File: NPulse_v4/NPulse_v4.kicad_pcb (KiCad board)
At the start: 4 copper layers, 39.8 x 72.5 mm, 163 parts, among them IC1 TXU0202QDCUR, IC2 DRV8220DSGR, IC3 DRV8220DSGR, IC4 DRV8220DSGR, IC5 DRV8220DSGR, IC6 DRV8220DSGR, IC7 DRV8220DSGR, IC8 DRV8220DSGR, IC9 DRV8220DSGR, J10 Conn_02x05_Odd_Even, J2 Conn_01x04_Pin, J3 Conn_01x06_Pin, J4 Conn_01x04_Pin, J5 Conn_02x05_Odd_Even, J6 Conn_02x05_Odd_Even, J7 Conn_02x05_Odd_Even, J8 Conn_02x05_Odd_Even, J9 Conn_02x05_Odd_Even, Q1 PMOS, Q2 NMOS, SW1 SW_Push, SW2 SW_SPDT, U1 STM32G484METx, U10 TPS7A0533PDBZ, U2 SN74LVC002, U3 SN74LVC002, U4 SN74LVC002, U5 SN74LVC002, U6 SN74LVC002, U7 SN74LVC002, U8 SN74LVC002, U9 SN74LVC002, Y1 16MHz

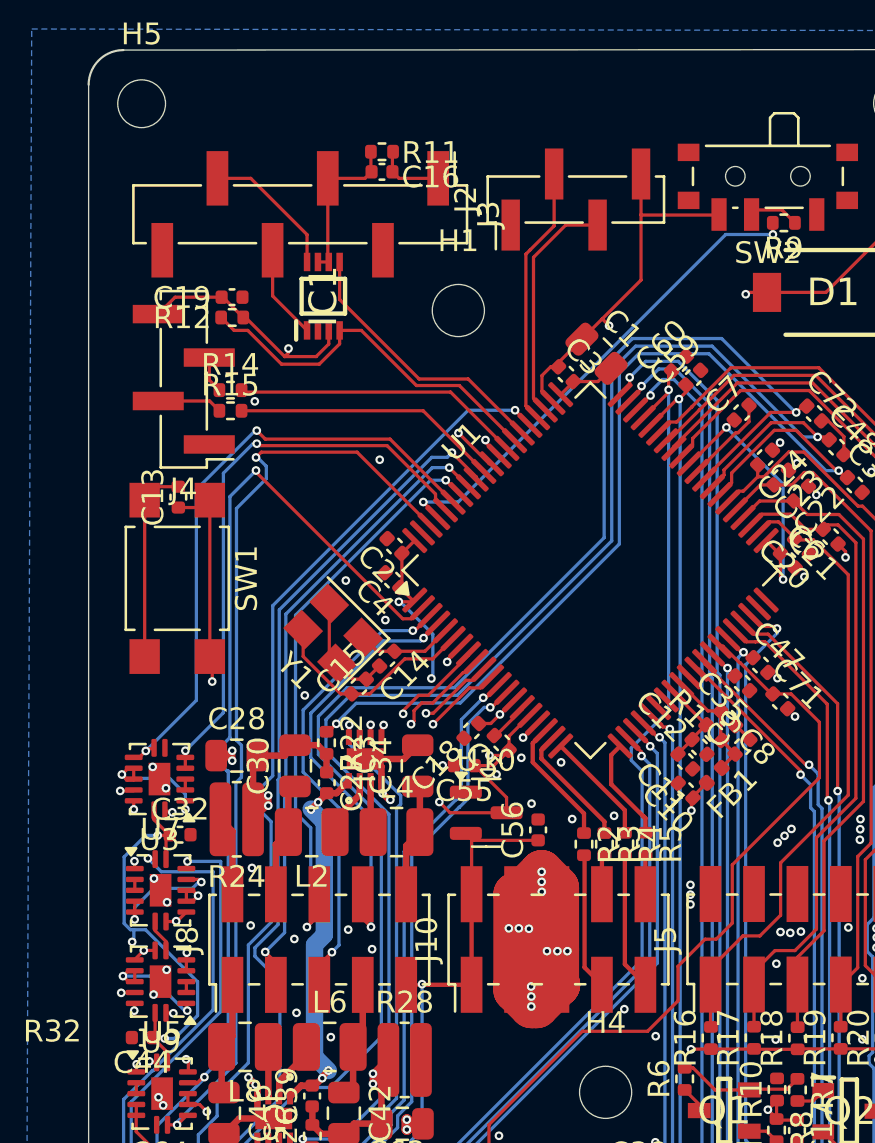
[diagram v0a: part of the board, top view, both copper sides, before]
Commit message: Correct LDO schematic and update connectors to through-hole footprints
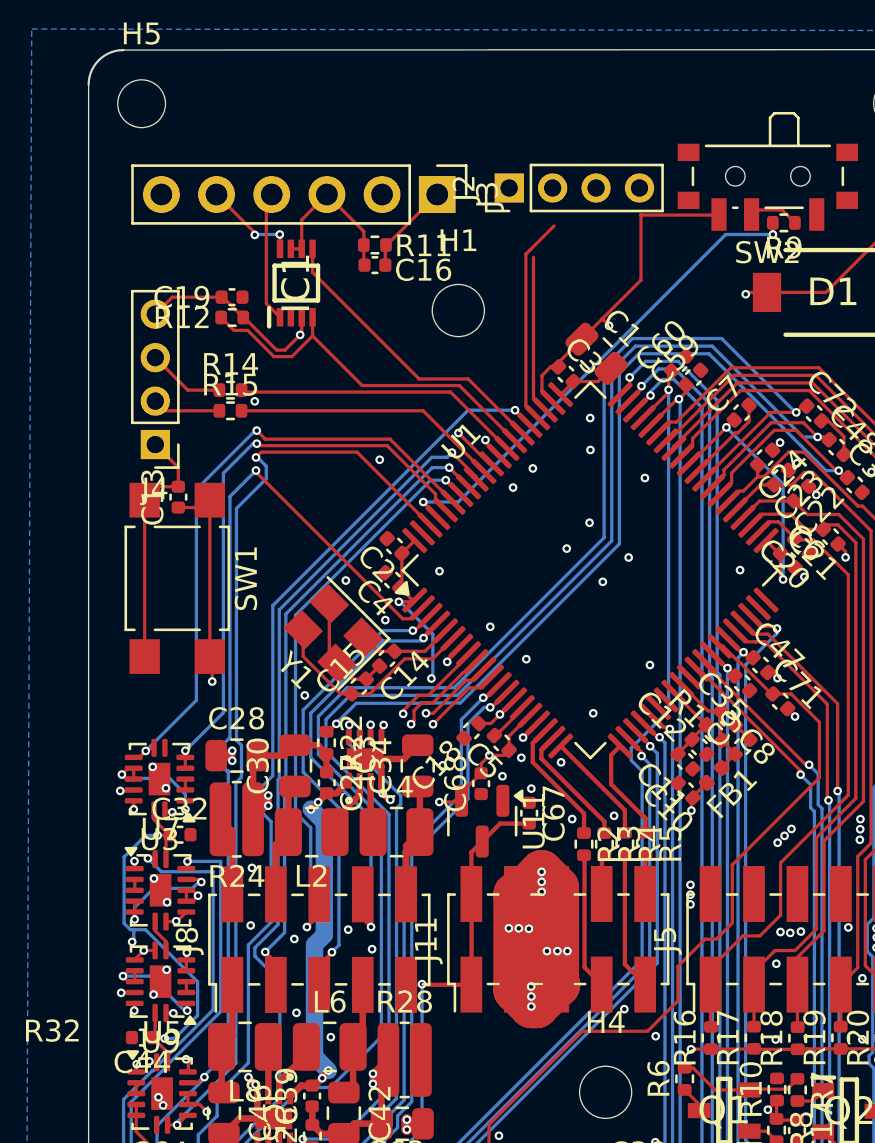
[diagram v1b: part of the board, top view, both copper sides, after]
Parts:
- removed C55, C56: 1uF, Capacitor_SMD:C_0402_1005Metric
- removed J10: Conn_02x05_Odd_Even, Connector_PinHeader_2.00mm:PinHeader_2x05_P2.00mm_Vertical_SMD
- removed U10: TPS7A0533PDBZ, Package_TO_SOT_SMD:SOT-23
- added C67: 1uF, Capacitor_SMD:C_0402_1005Metric, F.Cu at (173.7, 100.3)
- added C68: 1uF, Capacitor_SMD:C_0402_1005Metric, F.Cu at (171.4, 98.9)
- added J11: Conn_02x05_Odd_Even, Connector_PinHeader_2.00mm:PinHeader_2x05_P2.00mm_Vertical_SMD, F.Cu at (175.0, 106.1)
- added U11: TPS7A0533PDBZ, Package_TO_SOT_SMD:SOT-23, F.Cu at (171.5, 100.7)
- J2, J4: footprint Connector_PinHeader_2.00mm:PinHeader_1x04_P2.00mm_Vertical_SMD_Pin1Left -> Connector_PinHeader_2.00mm:PinHeader_1x04_P2.00mm_Vertical
- J3: footprint Connector_PinHeader_2.54mm:PinHeader_1x06_P2.54mm_Vertical_SMD_Pin1Left -> Connector_PinHeader_2.54mm:PinHeader_1x06_P2.54mm_Vertical
- moved J3 6.38 mm to (169.4, 71.8)
- moved R11 4.31 mm to (166.6, 74.1)
- moved C16 4.31 mm to (166.6, 75.1)
- moved J4 3.28 mm to (156.4, 83.3)
- moved J2 3.12 mm to (172.7, 71.5)
- moved IC1 1.38 mm to (162.9, 75.9)
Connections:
- IC2 pad 9: pin4_1 -> (no net)
- IC3 pad 9: pin4_5 -> (no net)
- IC4 pad 9: pin4_2 -> (no net)
- IC5 pad 9: pin4_6 -> (no net)
- IC6 pad 9: pin4_3 -> (no net)
- IC7 pad 9: pin4_7 -> (no net)
- IC8 pad 9: pin4_4 -> (no net)
- IC9 pad 9: pin4_8 -> (no net)
- U2 pad 15: GND -> (no net)
- U3 pad 15: GND -> (no net)
- U4 pad 15: GND -> (no net)
- U5 pad 15: GND -> (no net)
- U6 pad 15: GND -> (no net)
- U7 pad 15: GND -> (no net)
- U8 pad 15: GND -> (no net)
- U9 pad 15: GND -> (no net)
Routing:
- net +3.3V: track 205.5 -> 197.5 mm
- net /SWDIO: track 10.8 -> 7.25 mm
- net GND: track 57.1 -> 60.5 mm, vias 78 -> 93
- net /SWCLK: track 12.0 -> 9.59 mm
- net /RX: track 6.46 -> 4.41 mm, vias 0 -> 2
- net Net-(J4-Pin_3): track 1.69 -> 3.57 mm
- net /TX: track 4.35 -> 6.01 mm
- net +5V: track 56.4 -> 55.1 mm
- net /TX_UART4: track 12.7 -> 13.8 mm

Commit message: convert pin headers to 2.54mm
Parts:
- removed J3: Conn_01x06_Pin, Connector_PinHeader_2.54mm:PinHeader_1x06_P2.54mm_Vertical
- added J1: USB-to-UART, Connector_PinHeader_2.54mm:PinHeader_1x04_P2.54mm_Vertical, F.Cu at (166.5, 71.8)
- J2, J4: footprint Connector_PinHeader_2.00mm:PinHeader_1x04_P2.00mm_Vertical -> Connector_PinHeader_2.54mm:PinHeader_1x04_P2.54mm_Vertical
- moved J2 2.04 mm to (170.7, 71.7)
- moved J4 0.44 mm to (156.7, 83.0)
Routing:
- net /SWDIO: track 7.25 -> 11.1 mm
- net +3.3V: track 197.5 -> 199.3 mm
- net /SWCLK: track 9.59 -> 10.7 mm
